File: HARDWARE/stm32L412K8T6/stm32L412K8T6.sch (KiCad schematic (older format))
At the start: 25 parts, among them J1 Conn_01x02, J2 Conn_01x03_Male, J4 Conn_01x03_Male, J5 Conn_01x03_Male, J6 Conn_01x03_Male, SW1 SW_Push, U1 STM32L011K3Tx, U2 AMS1117-3.3, Y1 Crystal

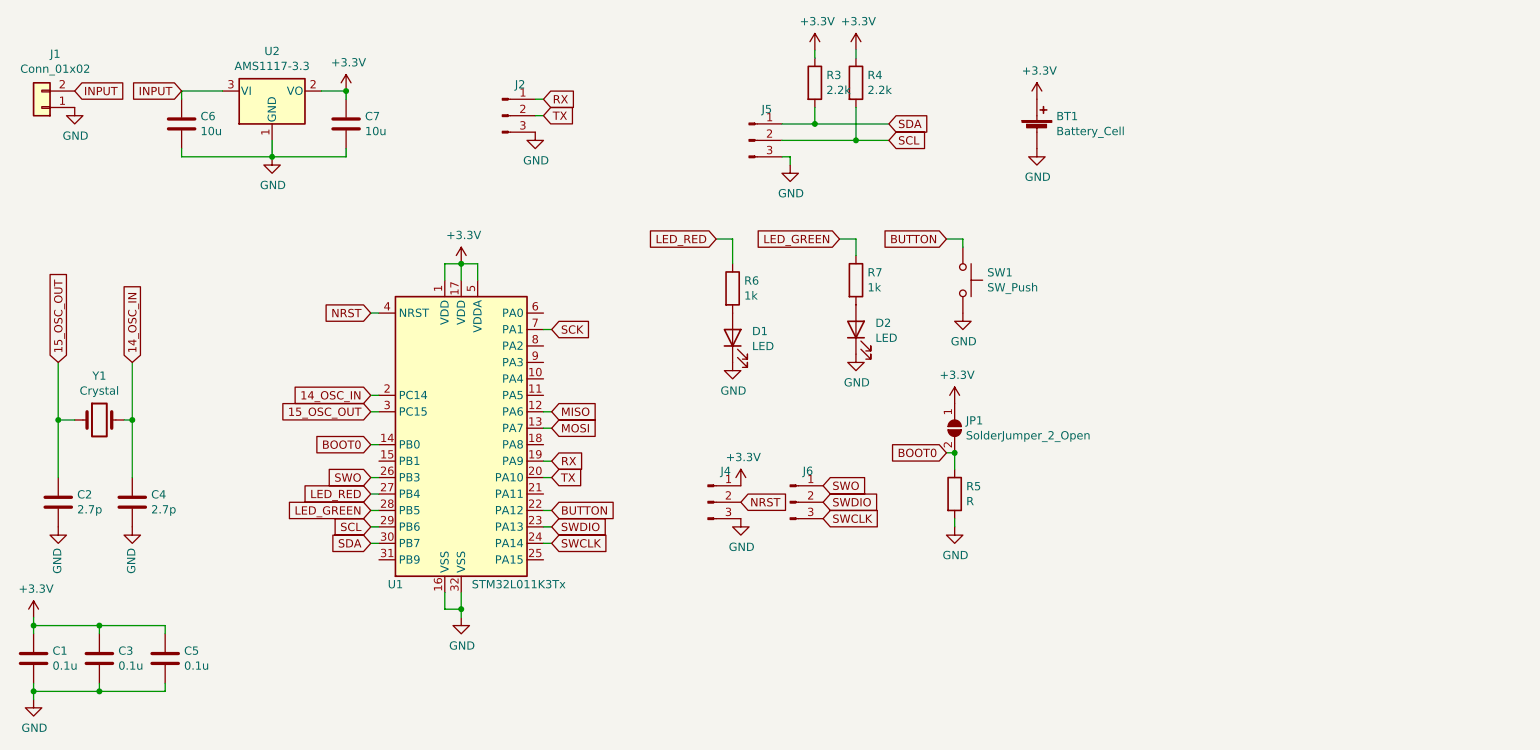
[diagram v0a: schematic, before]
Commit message: fail in processing gerber, create a new board
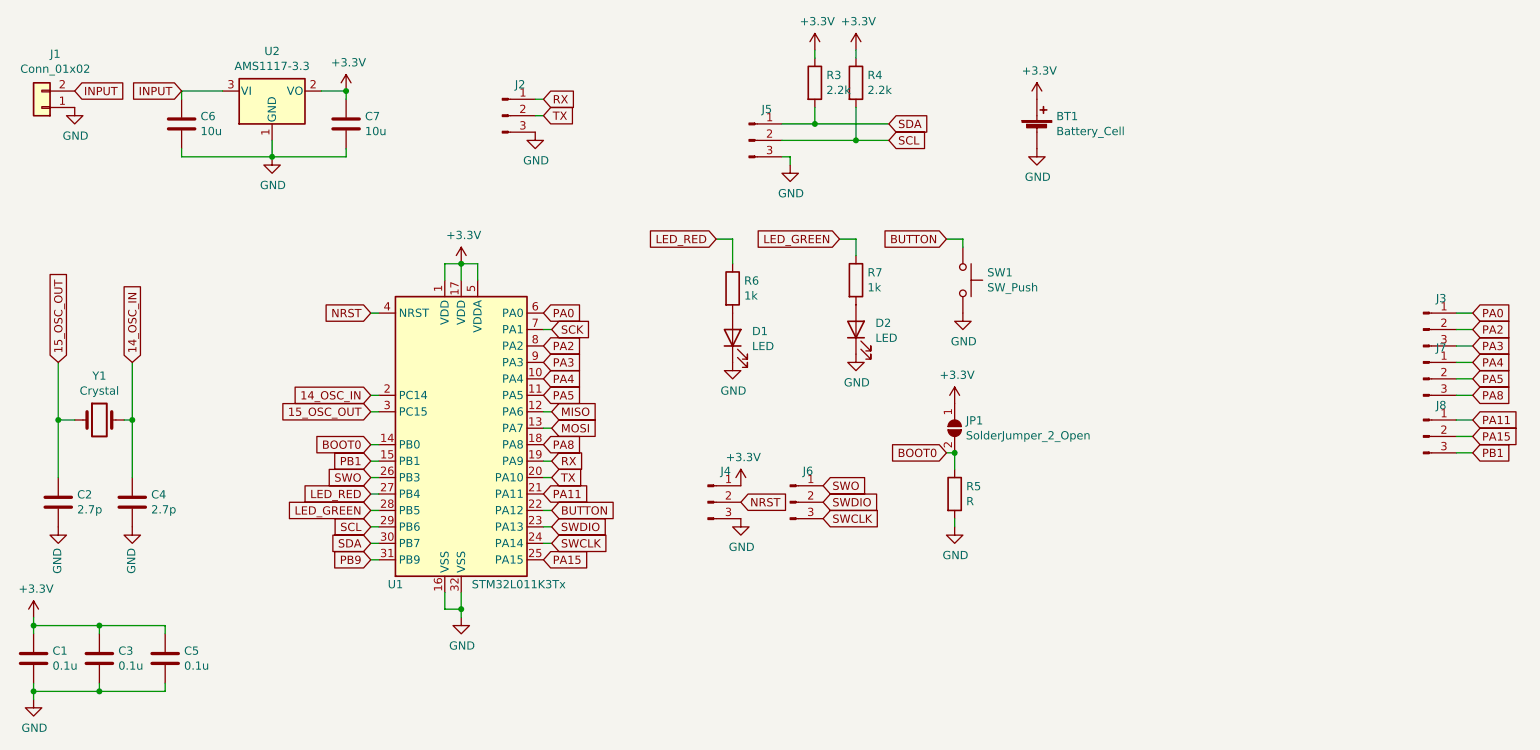
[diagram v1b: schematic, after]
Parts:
- added J3, J7, J8: Conn_01x03_Male, Connector_PinSocket_2.54mm:PinSocket_1x03_P2.54mm_Vertical_SMD_Pin1Right, symbol Connector:Conn_01x03_Male
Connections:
- net PA4: now reaches U1.10 (PA4)
- net PA4: now also J7.1 (Pin_1)
- net PA5: now reaches U1.11 (PA5)
- net PA5: now also J7.2 (Pin_2)
- net PB1: now reaches U1.15 (PB1)
- net PB1: now also J8.3 (Pin_3)
- net PA8: now reaches U1.18 (PA8)
- net PA8: now also J7.3 (Pin_3)
- net PA11: now reaches U1.21 (PA11)
- net PA11: now also J8.1 (Pin_1)
- net PA15: now reaches U1.25 (PA15)
- net PA15: now also J8.2 (Pin_2)
- net PB9: now reaches U1.31 (PB9)
- net PA0: now reaches U1.6 (PA0)
- net PA0: now also J3.1 (Pin_1)
- net PA2: now reaches U1.8 (PA2)
- net PA2: now also J3.2 (Pin_2)
- net PA3: now reaches U1.9 (PA3)
- net PA3: now also J3.3 (Pin_3)
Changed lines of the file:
@@
 	1    0    0    -1
 $EndComp
+$Comp
+L Connector:Conn_01x03_Male J3
+U 1 1 5FFB38F8
+P 9500 2500
+F 0 "J3" H 9608 2689 50  0000 C CNN
+F 1 "Conn_01x03_Male" H 9608 2690 50  0001 C CNN
+F 2 "Connector_PinSocket_2.54mm:PinSocket_1x03_P2.54mm_Vertical_SMD_Pin1Right" H 9500 2500 50  0001 C CNN
+F 3 "~" H 9500 2500 50  0001 C CNN
+	1    9500 2500
+	1    0    0    -1
+$EndComp
+Text GLabel 4150 2600 2    50   Input ~ 0
+PA2
+Text GLabel 4150 2700 2    50   Input ~ 0
+PA3
+Text GLabel 4150 2800 2    50   Input ~ 0
+PA4
+Text GLabel 4150 2900 2    50   Input ~ 0
+PA5
+Text GLabel 4150 2400 2    50   Input ~ 0
+PA0
+Text GLabel 4150 3200 2    50   Input ~ 0
+PA8
+Text GLabel 4150 3500 2    50   Input ~ 0
+PA11
+Text GLabel 9800 2500 2    50   Input ~ 0
+PA2
+Text GLabel 9800 2600 2    50   Input ~ 0
+PA3
+Text GLabel 9800 2700 2    50   Input ~ 0
+PA4
+Text GLabel 9800 2800 2    50   Input ~ 0
+PA5
+Text GLabel 9800 2400 2    50   Input ~ 0
+PA0
+Text GLabel 9800 2900 2    50   Input ~ 0
+PA8
+Text GLabel 9800 3050 2    50   Input ~ 0
+PA11
+$Comp
+L Connector:Conn_01x03_Male J7
+U 1 1 5FFBA7BE
+P 9500 2800
+F 0 "J7" H 9608 2989 50  0000 C CNN
+F 1 "Conn_01x03_Male" H 9608 2990 50  0001 C CNN
+F 2 "Connector_PinSocket_2.54mm:PinSocket_1x03_P2.54mm_Vertical_SMD_Pin1Right" H 9500 2800 50  0001 C CNN
+F 3 "~" H 9500 2800 50  0001 C CNN
+	1    9500 2800
+	1    0    0    -1
+$EndComp
+Wire Wire Line
+	9700 2400 9800 2400
+Wire Wire Line
+	9800 2500 9700 2500
+Wire Wire Line
+	9700 2600 9800 2600
+Wire Wire Line
+	9800 2700 9700 2700
+Wire Wire Line
+	9700 2800 9800 2800
+Wire Wire Line
+	9700 2900 9800 2900
+Text GLabel 4150 3900 2    50   Input ~ 0
+PA15
+Text GLabel 9800 3150 2    50   Input ~ 0
+PA15
+Text GLabel 3100 3900 0    50   Input ~ 0
+PB9
+Wire Wire Line
+	3150 3900 3100 3900
+Text GLabel 3100 3300 0    50   Input ~ 0
+PB1
+Wire Wire Line
+	3100 3300 3150 3300
+Text GLabel 9800 3250 2    50   Input ~ 0
+PB1
+$Comp
+L Connector:Conn_01x03_Male J8
+U 1 1 5FFD3D3C
+P 9500 3150
+F 0 "J8" H 9608 3339 50  0000 C CNN
+F 1 "Conn_01x03_Male" H 9608 3340 50  0001 C CNN
+F 2 "Connector_PinSocket_2.54mm:PinSocket_1x03_P2.54mm_Vertical_SMD_Pin1Right" H 9500 3150 50  0001 C CNN
+F 3 "~" H 9500 3150 50  0001 C CNN
+	1    9500 3150
+	1    0    0    -1
+$EndComp
+Wire Wire Line
+	9800 3050 9700 3050
+Wire Wire Line
+	9700 3150 9800 3150
+Wire Wire Line
+	9700 3250 9800 3250
 $EndSCHEMATC
